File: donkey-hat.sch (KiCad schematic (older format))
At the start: 51 parts, among them J1 5V, J14 NEOPIXEL, J15 MPU-9250, J16 4, J17 5, J18 6, J19 7, J2 Raspberry_Pi_2_3, J24 3mm_Mount, J25 3mm_Mount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

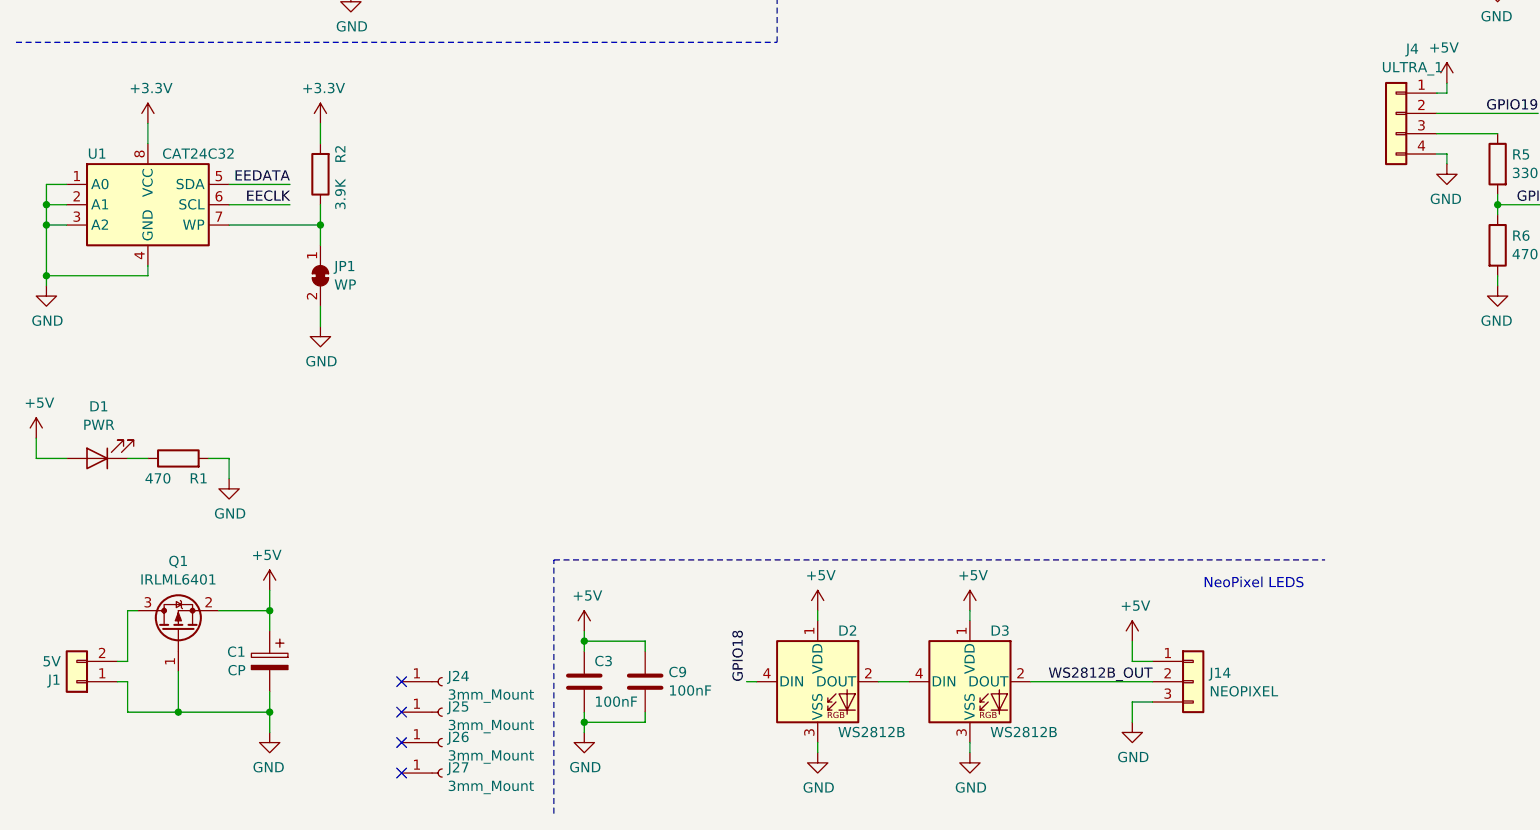
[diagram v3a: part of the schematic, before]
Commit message: Added 5v regulator
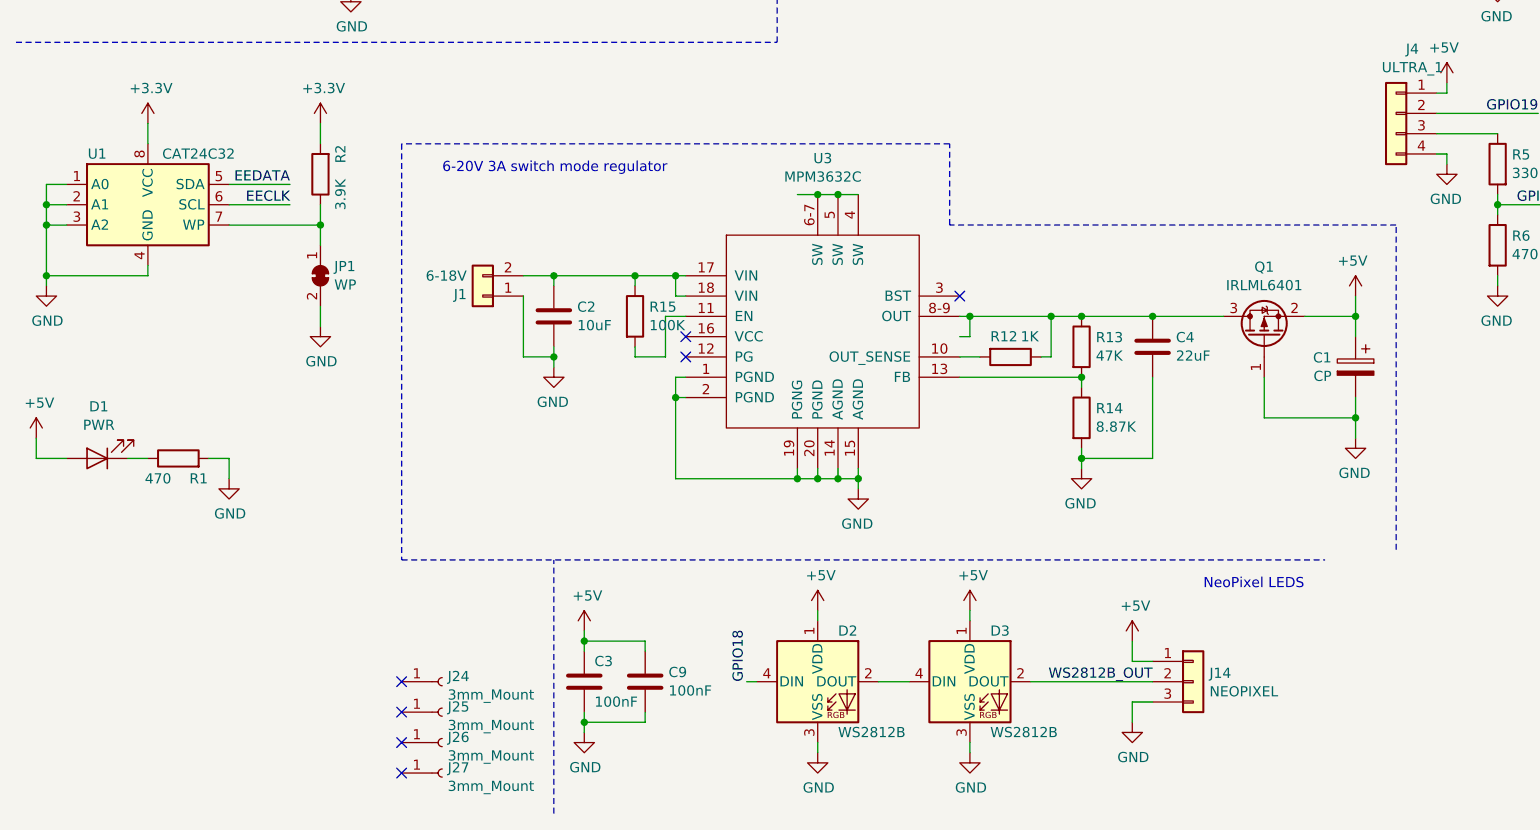
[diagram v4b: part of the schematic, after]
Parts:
- added C2: 10uF, Capacitor_SMD:C_0603_1608Metric_Pad1.05x0.95mm_HandSolder, symbol Device:C
- added C4: 22uF, Capacitor_SMD:C_0603_1608Metric_Pad1.05x0.95mm_HandSolder, symbol Device:C
- added R12: 1K, Resistor_SMD:R_0603_1608Metric_Pad1.05x0.95mm_HandSolder, symbol Device:R
- added R13: 47K, Resistor_SMD:R_0603_1608Metric_Pad1.05x0.95mm_HandSolder, symbol Device:R
- added R14: 8.87K, Resistor_SMD:R_0603_1608Metric_Pad1.05x0.95mm_HandSolder, symbol Device:R
- added R15: 100K, Resistor_SMD:R_0603_1608Metric_Pad1.05x0.95mm_HandSolder, symbol Device:R
- added U3: MPM3632C, libs:mpm3632c, symbol donkey-hat:MPM3632C
- J1: value 5V -> 6-18V
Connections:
- net GND: now also C2.2, C4.2, R14.2, U3.1 (PGND), U3.14 (AGND), U3.15 (AGND), U3.19 (PGNG), U3.2 (PGND), U3.20 (PGND)
- net at J1.2 (Pin_2): now also C2.1, R15.1, U3.17 (VIN), U3.18 (VIN); no longer Q1.3 (D)
- new net: R12.2, U3.10 (OUT_SENSE)
- new net: R15.2, U3.11 (EN)
- new net: R13.2, R14.1, U3.13 (FB)
- new net: U3.4 (SW), U3.5 (SW), U3.6-7 (SW)
- new net: C4.1, Q1.3 (D), R12.1, R13.1, U3.8-9 (OUT)
- no-connect marks 7 -> 10
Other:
- note added: "6-20V 3A switch mode regulator\n"
- moved on the sheet: C1, J1, Q1

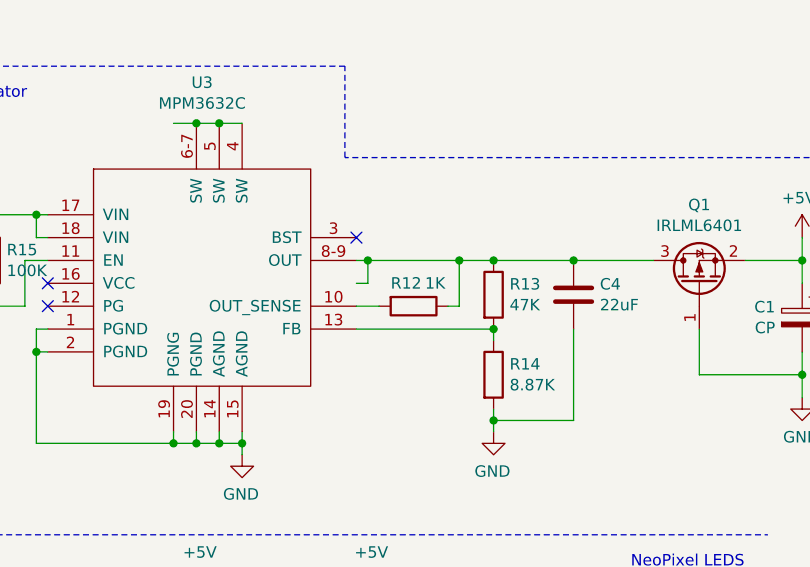
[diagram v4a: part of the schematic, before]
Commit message: Updated to 0.3mm Vias.
Makes pcbway a lot cheaper to order from.
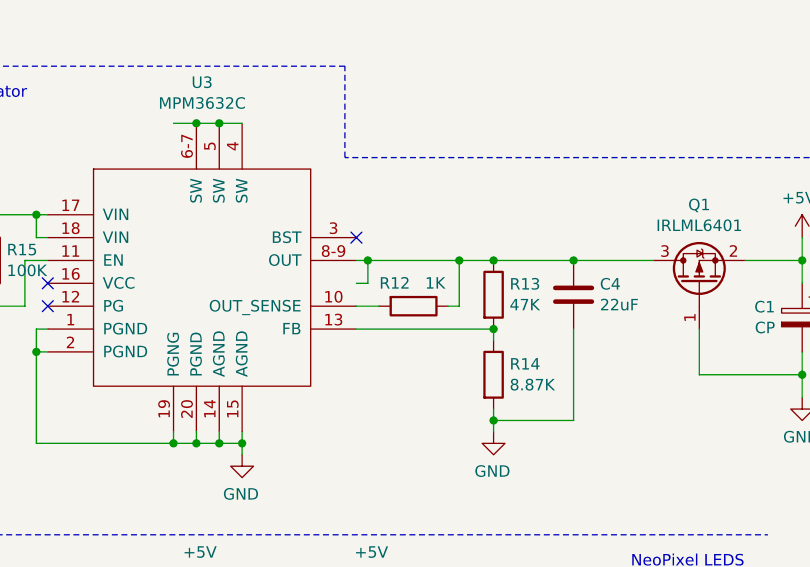
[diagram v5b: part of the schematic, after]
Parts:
- C2, C4: footprint Capacitor_SMD:C_0603_1608Metric_Pad1.05x0.95mm_HandSolder -> Capacitor_SMD:C_1206_3216Metric_Pad1.42x1.75mm_HandSolder
- Q1: Link (none) -> https://www.digikey.com.au/product-detail/en/infineon-techn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
- U1: Link (none) -> https://www.digikey.com.au/product-detail/en/on-semiconduct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
- U2: Link (none) -> https://www.digikey.com.au/product-detail/en/nxp-usa-inc/PC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
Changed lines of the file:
@@
 F 2 "Package_SO:TSSOP-28_4.4x9.7mm_P0.65mm" H 9825 2075 50  0001 L CNN
 F 3 "http://www.nxp.com/documents/data_sheet/PCA9685.pdf" H 9400 3750 50  0001 C CNN
+F 4 "https://www.digikey.com.au/product-detail/en/nxp-usa-inc/PCA9685PW118/568-11925-1-ND/5221902" H 9800 3050 50  0001 C CNN "Link"
 	1    9800 3050
 	1    0    0    -1
@@
 F 2 "Package_SO:SOIC-8_3.9x4.9mm_P1.27mm" H 1150 4800 50  0001 C CNN
 F 3 "https://www.onsemi.cn/PowerSolutions/document/CAT24C256-D.PDF" H 1150 4800 50  0001 C CNN
+F 4 "https://www.digikey.com.au/product-detail/en/on-semiconductor/CAT24C32WI-GT3/CAT24C32WI-GT3CT-ND/1631159" H 1150 4800 50  0001 C CNN "Link"
 	1    1150 4800
 	1    0    0    -1
@@
 F 2 "Package_TO_SOT_SMD:SOT-23_Handsoldering" H 6850 5375 50  0001 L CIN
 F 3 "https://www.infineon.com/dgdl/irlml6402pbf.pdf?fileId=5546d462533600a401535668d5c2263c" H 6650 5450 50  0001 L CNN
+F 4 "https://www.digikey.com.au/product-detail/en/infineon-technologies/IRLML6401TRPBF/IRLML6401PBFCT-ND/812509" V 6650 5450 50  0001 C CNN "Link"
 	1    6650 5450
 	0    -1   -1   0
@@
 U 1 1 5C301B56
 P 5400 5550
-F 0 "R12" V 5300 5450 50  0000 L CNN
+F 0 "R12" V 5300 5400 50  0000 L CNN
 F 1 "1K" V 5300 5600 50  0000 L CNN
 F 2 "Resistor_SMD:R_0603_1608Metric_Pad1.05x0.95mm_HandSolder" V 5330 5550 50  0001 C CNN
@@
 F 0 "C4" H 6215 5546 50  0000 L CNN
 F 1 "22uF" H 6215 5455 50  0000 L CNN
-F 2 "Capacitor_SMD:C_0603_1608Metric_Pad1.05x0.95mm_HandSolder" H 6138 5350 50  0001 C CNN
+F 2 "Capacitor_SMD:C_1206_3216Metric_Pad1.42x1.75mm_HandSolder" H 6138 5350 50  0001 C CNN
 F 3 "~" H 6100 5500 50  0001 C CNN
 	1    6100 5500
@@
 F 0 "C2" H 3265 5396 50  0000 L CNN
 F 1 "10uF" H 3265 5305 50  0000 L CNN
-F 2 "Capacitor_SMD:C_0603_1608Metric_Pad1.05x0.95mm_HandSolder" H 3188 5200 50  0001 C CNN
+F 2 "Capacitor_SMD:C_1206_3216Metric_Pad1.42x1.75mm_HandSolder" H 3188 5200 50  0001 C CNN
 F 3 "~" H 3150 5350 50  0001 C CNN
 	1    3150 5350

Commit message: Adding component footprints
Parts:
- C2, C4: Package (none) -> 1206
- C3, C7, C8, C9, D1, R1, R10, R11, R12, R13, R14, R15, R2, R3, R4, R5, R6, R7, R8, R9: Package (none) -> 0603
- D2, D3, RN1, RN2, RN5, RN6: Package (none) -> SMD
- Q1: Package (none) -> SOT-23
- U1: Package (none) -> 8-SOIC
- U2: Package (none) -> 28-TSSOP
- U3: Package (none) -> 20-QFN
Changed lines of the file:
@@
 F 3 "http://www.nxp.com/documents/data_sheet/PCA9685.pdf" H 9400 3750 50  0001 C CNN
 F 4 "https://www.digikey.com.au/product-detail/en/nxp-usa-inc/PCA9685PW118/568-11925-1-ND/5221902" H 9800 3050 50  0001 C CNN "Link"
+F 5 "28-TSSOP" H 0   0   50  0001 C CNN "Package"
 	1    9800 3050
 	1    0    0    -1
@@
 F 3 "https://www.onsemi.cn/PowerSolutions/document/CAT24C256-D.PDF" H 1150 4800 50  0001 C CNN
 F 4 "https://www.digikey.com.au/product-detail/en/on-semiconductor/CAT24C32WI-GT3/CAT24C32WI-GT3CT-ND/1631159" H 1150 4800 50  0001 C CNN "Link"
+F 5 "8-SOIC" H 0   0   50  0001 C CNN "Package"
 	1    1150 4800
 	1    0    0    -1
@@
 F 2 "Capacitor_SMD:C_0603_1608Metric_Pad1.05x0.95mm_HandSolder" H 8938 1150 50  0001 C CNN
 F 3 "~" H 8900 1300 50  0001 C CNN
+F 4 "0603" H 0   0   50  0001 C CNN "Package"
 	1    8900 1300
 	1    0    0    -1
@@
 F 2 "Resistor_SMD:R_0603_1608Metric_Pad1.05x0.95mm_HandSolder" V 8680 2850 50  0001 C CNN
 F 3 "~" H 8750 2850 50  0001 C CNN
+F 4 "0603" H 0   0   50  0001 C CNN "Package"
 	1    8750 2850
 	1    0    0    -1
@@
 F 3 "~" H 4900 1500 50  0001 C CNN
 F 4 "https://www.aliexpress.com/item/200PCS-0603-2X4-220R-220-ohm-Marking-221-SMD-Network-Resistor-array-0603-8P4R-2-4P/32845505270.html?spm=2114.search0104.3.35.c74a11b9SNycSm&ws_ab_test=searchweb0_0,searchweb201602_2_10065_10068_10130_10547_319_317_10548_10696_453_10084_454_10083_10618_10307_537_536_10131_10132_10133_10059_10884_10887_100031_321_322_10103,searchweb201603_51,ppcSwitch_0&algo_expid=516fab08-5bb7-441c-804a-744d42f8303d-5&algo_pvid=516fab08-5bb7-441c-804a-744d42f8303d" V 4900 1500 50  0001 C CNN "Link"
+F 5 "SMD" H 0   0   50  0001 C CNN "Package"
 	1    4900 1500
 	0    1    1    0
@@
 F 2 "Resistor_SMD:R_Array_Convex_4x0603" V 7125 1500 50  0001 C CNN
 F 3 "~" H 6850 1500 50  0001 C CNN
+F 4 "SMD" H 0   0   50  0001 C CNN "Package"
 	1    6850 1500
 	0    1    1    0
@@
 F 2 "Resistor_SMD:R_0603_1608Metric_Pad1.05x0.95mm_HandSolder" V 1930 4650 50  0001 C CNN
 F 3 "~" H 2000 4650 50  0001 C CNN
+F 4 "0603" H 0   0   50  0001 C CNN "Package"
 	1    2000 4650
 	-1   0    0    1
@@
 F 2 "LED_SMD:LED_0603_1608Metric_Pad1.05x0.95mm_HandSolder" H 900 6050 50  0001 C CNN
 F 3 "~" H 900 6050 50  0001 C CNN
+F 4 "0603" H 0   0   50  0001 C CNN "Package"
 	1    900  6050
 	-1   0    0    1
@@
 F 2 "Resistor_SMD:R_0603_1608Metric_Pad1.05x0.95mm_HandSolder" V 1230 6050 50  0001 C CNN
 F 3 "~" H 1300 6050 50  0001 C CNN
+F 4 "0603" H 0   0   50  0001 C CNN "Package"
 	1    1300 6050
 	0    -1   -1   0
@@
 F 3 "https://www.infineon.com/dgdl/irlml6402pbf.pdf?fileId=5546d462533600a401535668d5c2263c" H 6650 5450 50  0001 L CNN
 F 4 "https://www.digikey.com.au/product-detail/en/infineon-technologies/IRLML6401TRPBF/IRLML6401PBFCT-ND/812509" V 6650 5450 50  0001 C CNN "Link"
+F 5 "SOT-23" H 0   0   50  0001 C CNN "Package"
 	1    6650 5450
 	0    -1   -1   0
@@
 F 2 "LED_SMD:LED_WS2812B_PLCC4_5.0x5.0mm_P3.2mm" H 4500 6850 50  0001 L TNN
 F 3 "https://cdn-shop.adafruit.com/datasheets/WS2812B.pdf" H 4550 6775 50  0001 L TNN
+F 4 "SMD" H 0   0   50  0001 C CNN "Package"
 	1    4450 7150
 	1    0    0    -1
@@
 F 2 "LED_SMD:LED_WS2812B_PLCC4_5.0x5.0mm_P3.2mm" H 5250 6850 50  0001 L TNN
 F 3 "https://cdn-shop.adafruit.com/datasheets/WS2812B.pdf" H 5300 6775 50  0001 L TNN
+F 4 "SMD" H 0   0   50  0001 C CNN "Package"
 	1    5200 7150
 	1    0    0    -1
@@
 F 2 "Capacitor_SMD:C_0603_1608Metric_Pad1.05x0.95mm_HandSolder" H 3338 7000 50  0001 C CNN
 F 3 "~" H 3300 7150 50  0001 C CNN
+F 4 "0603" H 0   0   50  0001 C CNN "Package"
 	1    3300 7150
 	1    0    0    -1
@@
 F 2 "Capacitor_SMD:C_0603_1608Metric_Pad1.05x0.95mm_HandSolder" H 9388 1150 50  0001 C CNN
 F 3 "~" H 9350 1300 50  0001 C CNN
+F 4 "0603" H 0   0   50  0001 C CNN "Package"
 	1    9350 1300
 	1    0    0    -1
@@
 F 2 "Resistor_SMD:R_Array_Convex_4x0603" V 10575 5750 50  0001 C CNN
 F 3 "~" H 10300 5750 50  0001 C CNN
+F 4 "SMD" H 0   0   50  0001 C CNN "Package"
 	1    10300 5750
 	0    1    -1   0
@@
 F 2 "Resistor_SMD:R_Array_Convex_4x0603" V 10575 5100 50  0001 C CNN
 F 3 "~" H 10300 5100 50  0001 C CNN
+F 4 "SMD" H 0   0   50  0001 C CNN "Package"
 	1    10300 5100
 	0    1    -1   0
@@
 F 2 "Capacitor_SMD:C_0603_1608Metric_Pad1.05x0.95mm_HandSolder" H 3638 7000 50  0001 C CNN
 F 3 "~" H 3600 7150 50  0001 C CNN
+F 4 "0603" H 0   0   50  0001 C CNN "Package"
 	1    3600 7150
 	1    0    0    -1
@@
 F 2 "Resistor_SMD:R_0603_1608Metric_Pad1.05x0.95mm_HandSolder" V 7730 3100 50  0001 C CNN
 F 3 "~" H 7800 3100 50  0001 C CNN
+F 4 "0603" H 0   0   50  0001 C CNN "Package"
 	1    7800 3100
 	-1   0    0    -1
@@
 F 2 "Resistor_SMD:R_0603_1608Metric_Pad1.05x0.95mm_HandSolder" V 7730 3500 50  0001 C CNN
 F 3 "~" H 7800 3500 50  0001 C CNN
+F 4 "0603" H 0   0   50  0001 C CNN "Package"
 	1    7800 3500
 	1    0    0    -1
@@
 F 2 "Resistor_SMD:R_0603_1608Metric_Pad1.05x0.95mm_HandSolder" V 7730 4600 50  0001 C CNN
 F 3 "~" H 7800 4600 50  0001 C CNN
+F 4 "0603" H 0   0   50  0001 C CNN "Package"
 	1    7800 4600
 	-1   0    0    -1
@@
 F 2 "Resistor_SMD:R_0603_1608Metric_Pad1.05x0.95mm_HandSolder" V 7730 5000 50  0001 C CNN
 F 3 "~" H 7800 5000 50  0001 C CNN
+F 4 "0603" H 0   0   50  0001 C CNN "Package"
 	1    7800 5000
 	1    0    0    -1
@@
 F 2 "Resistor_SMD:R_0603_1608Metric_Pad1.05x0.95mm_HandSolder" V 3030 1050 50  0001 C CNN
 F 3 "~" H 3100 1050 50  0001 C CNN
+F 4 "0603" H 3100 1050 50  0001 C CNN "Package"
 	1    3100 1050
 	1    0    0    -1
@@
 F 2 "Resistor_SMD:R_0603_1608Metric_Pad1.05x0.95mm_HandSolder" V 3330 1050 50  0001 C CNN
 F 3 "~" H 3400 1050 50  0001 C CNN
+F 4 "0603" H 3400 1050 50  0001 C CNN "Package"
 	1    3400 1050
 	1    0    0    -1
@@
 F 2 "Resistor_SMD:R_0603_1608Metric_Pad1.05x0.95mm_HandSolder" V 3630 1050 50  0001 C CNN
 F 3 "~" H 3700 1050 50  0001 C CNN
+F 4 "0603" H 0   0   50  0001 C CNN "Package"
 	1    3700 1050
 	1    0    0    -1
@@
 F 2 "Resistor_SMD:R_0603_1608Metric_Pad1.05x0.95mm_HandSolder" V 3930 1050 50  0001 C CNN
 F 3 "~" H 4000 1050 50  0001 C CNN
+F 4 "0603" H 0   0   50  0001 C CNN "Package"
 	1    4000 1050
 	1    0    0    -1
@@
 F 3 "https://media.monolithicpower.com/document/m/p/mpm3632c_r1.0.pdf" H 4500 5450 50  0001 C CNN
 F 4 "https://www.digikey.com/product-detail/en/monolithic-power-systems-inc/MPM3632CGQV-Z/1589-1955-1-ND/9637668" H 4500 5450 50  0001 C CNN "Link"
+F 5 "20-QFN" H 0   0   50  0001 C CNN "Package"
 	1    4500 5450
 	1    0    0    -1
@@
 F 2 "Resistor_SMD:R_0603_1608Metric_Pad1.05x0.95mm_HandSolder" V 5680 5850 50  0001 C CNN
 F 3 "~" H 5750 5850 50  0001 C CNN
+F 4 "0603" H 0   0   50  0001 C CNN "Package"
 	1    5750 5850
 	1    0    0    -1
@@
 F 2 "Resistor_SMD:R_0603_1608Metric_Pad1.05x0.95mm_HandSolder" V 5330 5550 50  0001 C CNN
 F 3 "~" H 5400 5550 50  0001 C CNN
+F 4 "0603" H 0   0   50  0001 C CNN "Package"
 	1    5400 5550
 	0    1    1    0
@@
 F 2 "Capacitor_SMD:C_1206_3216Metric_Pad1.42x1.75mm_HandSolder" H 6138 5350 50  0001 C CNN
 F 3 "~" H 6100 5500 50  0001 C CNN
+F 4 "1206" H 0   0   50  0001 C CNN "Package"
 	1    6100 5500
 	1    0    0    -1
@@
 F 2 "Resistor_SMD:R_0603_1608Metric_Pad1.05x0.95mm_HandSolder" V 5680 5500 50  0001 C CNN
 F 3 "~" H 5750 5500 50  0001 C CNN
+F 4 "0603" H 0   0   50  0001 C CNN "Package"
 	1    5750 5500
 	1    0    0    -1
@@
 F 2 "Capacitor_SMD:C_1206_3216Metric_Pad1.42x1.75mm_HandSolder" H 3188 5200 50  0001 C CNN
 F 3 "~" H 3150 5350 50  0001 C CNN
+F 4 "1206" H 0   0   50  0001 C CNN "Package"
 	1    3150 5350
 	1    0    0    -1
@@
 F 2 "Resistor_SMD:R_0603_1608Metric_Pad1.05x0.95mm_HandSolder" V 3480 5350 50  0001 C CNN
 F 3 "~" H 3550 5350 50  0001 C CNN
+F 4 "0603" H 0   0   50  0001 C CNN "Package"
 	1    3550 5350
 	1    0    0    -1
